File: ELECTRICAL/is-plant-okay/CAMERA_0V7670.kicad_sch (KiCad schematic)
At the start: 0 parts

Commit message: feat: add header pins for tft and camera
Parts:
- added J6: 10129381-918001BLF, is-plant-okay-foot:AMPHENOL_10129381-918001BLF, symbol is-plant-okay-lib:10129381-918001BLF
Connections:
- new net 3.3V: J6.01
- new net CAM_PWDN: J6.18
- new net CAM_RST: J6.17
- new net D0: J6.16
- new net D1: J6.15
- new net D2: J6.14
- new net D3: J6.13
- new net D4: J6.12
- new net D5: J6.11
- new net D6: J6.10
- new net D7: J6.09
- new net GND: J6.02
- new net HREF: J6.06
- new net PCLK: J6.07
- new net SIOC: J6.03
- new net SIOD: J6.04
- new net VSYNC: J6.05
- new net XCLK: J6.08

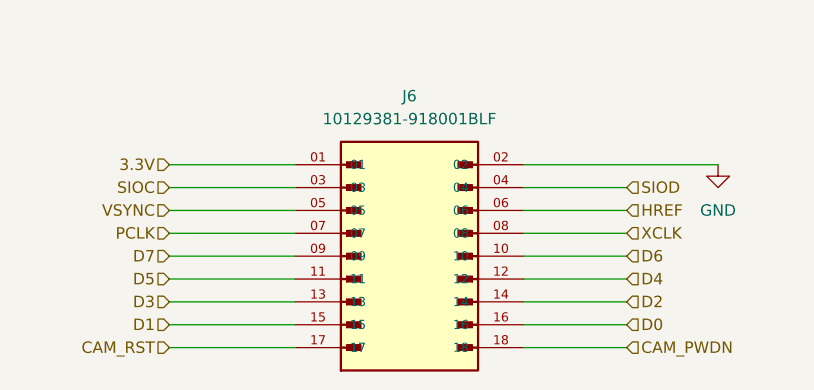
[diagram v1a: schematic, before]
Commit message: feat: add pins for mcu
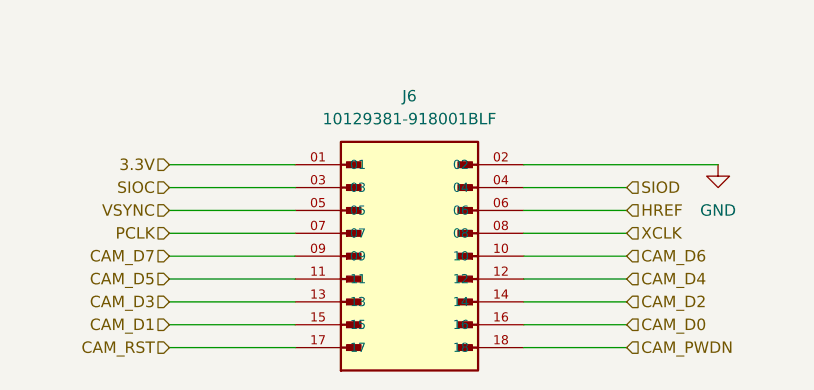
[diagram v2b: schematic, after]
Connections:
- net D0 renamed CAM_D0
- net D1 renamed CAM_D1
- net D2 renamed CAM_D2
- net D3 renamed CAM_D3
- net D4 renamed CAM_D4
- net D5 renamed CAM_D5
- net D6 renamed CAM_D6
- net D7 renamed CAM_D7
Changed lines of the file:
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@@
 		)
 	)
-	(hierarchical_label "D0"
+	(hierarchical_label "CAM_D0"
 		(shape input)
 		(at 173.99 107.95 0)
@@
 		)
 	)
-	(hierarchical_label "D6"
+	(hierarchical_label "CAM_D6"
 		(shape input)
 		(at 173.99 100.33 0)
@@
 		)
 	)
-	(hierarchical_label "D3"
+	(hierarchical_label "CAM_D3"
 		(shape input)
 		(at 123.19 105.41 180)
@@
 		)
 	)
-	(hierarchical_label "D5"
+	(hierarchical_label "CAM_D5"
 		(shape input)
 		(at 123.19 102.87 180)
@@
 		)
 	)
-	(hierarchical_label "D7"
+	(hierarchical_label "CAM_D7"
 		(shape input)
 		(at 123.19 100.33 180)
@@
 		)
 	)
-	(hierarchical_label "D1"
+	(hierarchical_label "CAM_D1"
 		(shape input)
 		(at 123.19 107.95 180)
@@
 		)
 	)
-	(hierarchical_label "D4"
+	(hierarchical_label "CAM_D4"
 		(shape input)
 		(at 173.99 102.87 0)
@@
 		)
 	)
-	(hierarchical_label "D2"
+	(hierarchical_label "CAM_D2"
 		(shape input)
 		(at 173.99 105.41 0)

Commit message: feat: finished schematics
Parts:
- added TP6: CAM_3.3V_TP, TestPoint:TestPoint_Keystone_5000-5004_Miniature, symbol Connector:TestPoint
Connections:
- net 3.3V: now also TP6.1
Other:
- note added: "OV7670 Datasheet: https://web.mit.edu/6.111/www/f2016/tools/OV7670_2006.pdf"
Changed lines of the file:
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@@
 	(generator_version "9.0")
 	(paper "A4")
+	(text "OV7670\nDatasheet: https://web.mit.edu/6.111/www/f2016/tools/OV7670_2006.pdf"
+		(exclude_from_sim no)
+		(at 149.606 76.454 0)
+		(effects
+			(font
+				(size 1.27 1.27)
+			)
+		)
+	)
+	(junction
+		(at 124.46 90.17)
+		(diameter 0)
+		(color 0 0 0 0)
+	)
 	(wire
 		(pts
@@
 	(wire
 		(pts
+			(xy 124.46 90.17) (xy 137.16 90.17)
+		)
+		(stroke
+			(width 0)
+			(type default)
+		)
+	)
+	(wire
+		(pts
 			(xy 123.19 92.71) (xy 137.16 92.71)
 		)
@@
 	(wire
 		(pts
-			(xy 123.19 90.17) (xy 137.16 90.17)
+			(xy 123.19 90.17) (xy 124.46 90.17)
 		)
 		(stroke
@@
 					(unit 1)
 				)
+			)
+		)
+	)
+	(symbol
+		(lib_id "Connector:TestPoint")
+		(at 124.46 90.17 0)
+		(unit 1)
+		(exclude_from_sim no)
+		(in_bom yes)
+		(on_board yes)
+		(dnp no)
+		(fields_autoplaced yes)
+		(property "Reference" "TP6"
+			(at 127 85.5979 0)
+			(effects
+				(font
+					(size 1.27 1.27)
+				)
+				(justify left)
+			)
+		)
+		(property "Value" "CAM_3.3V_TP"
+			(at 127 88.1379 0)
+			(effects
+				(font
+					(size 1.27 1.27)
+				)
+				(justify left)
+			)
+		)
+		(property "Footprint" "TestPoint:TestPoint_Keystone_5000-5004_Miniature"
+			(at 129.54 90.17 0)
+			(effects
+				(font
+					(size 1.27 1.27)
+				)
+				(hide yes)
+			)
+		)
+		(property "Datasheet" "~"
+			(at 129.54 90.17 0)
+			(effects
+				(font
+					(size 1.27 1.27)
+				)
+				(hide yes)
+			)
+		)
+		(property "Description" "test point"
+			(at 124.46 90.17 0)
+			(effects
+				(font
+					(size 1.27 1.27)
+				)
+				(hide yes)
+			)
+		)
+		(pin "1"
+		)
+		(instances
+			(project "is-plant-okay"
+				(path "/ac51c2f9-77a4-4b89-b63f-6e0ba02b1e45/620be07c-2bce-4383-9b50-1c824f90bb5c"
+					(reference "TP6")
+					(unit 1)
+				)
